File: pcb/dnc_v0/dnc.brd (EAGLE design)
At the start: 100 x 80 mm, 1 part

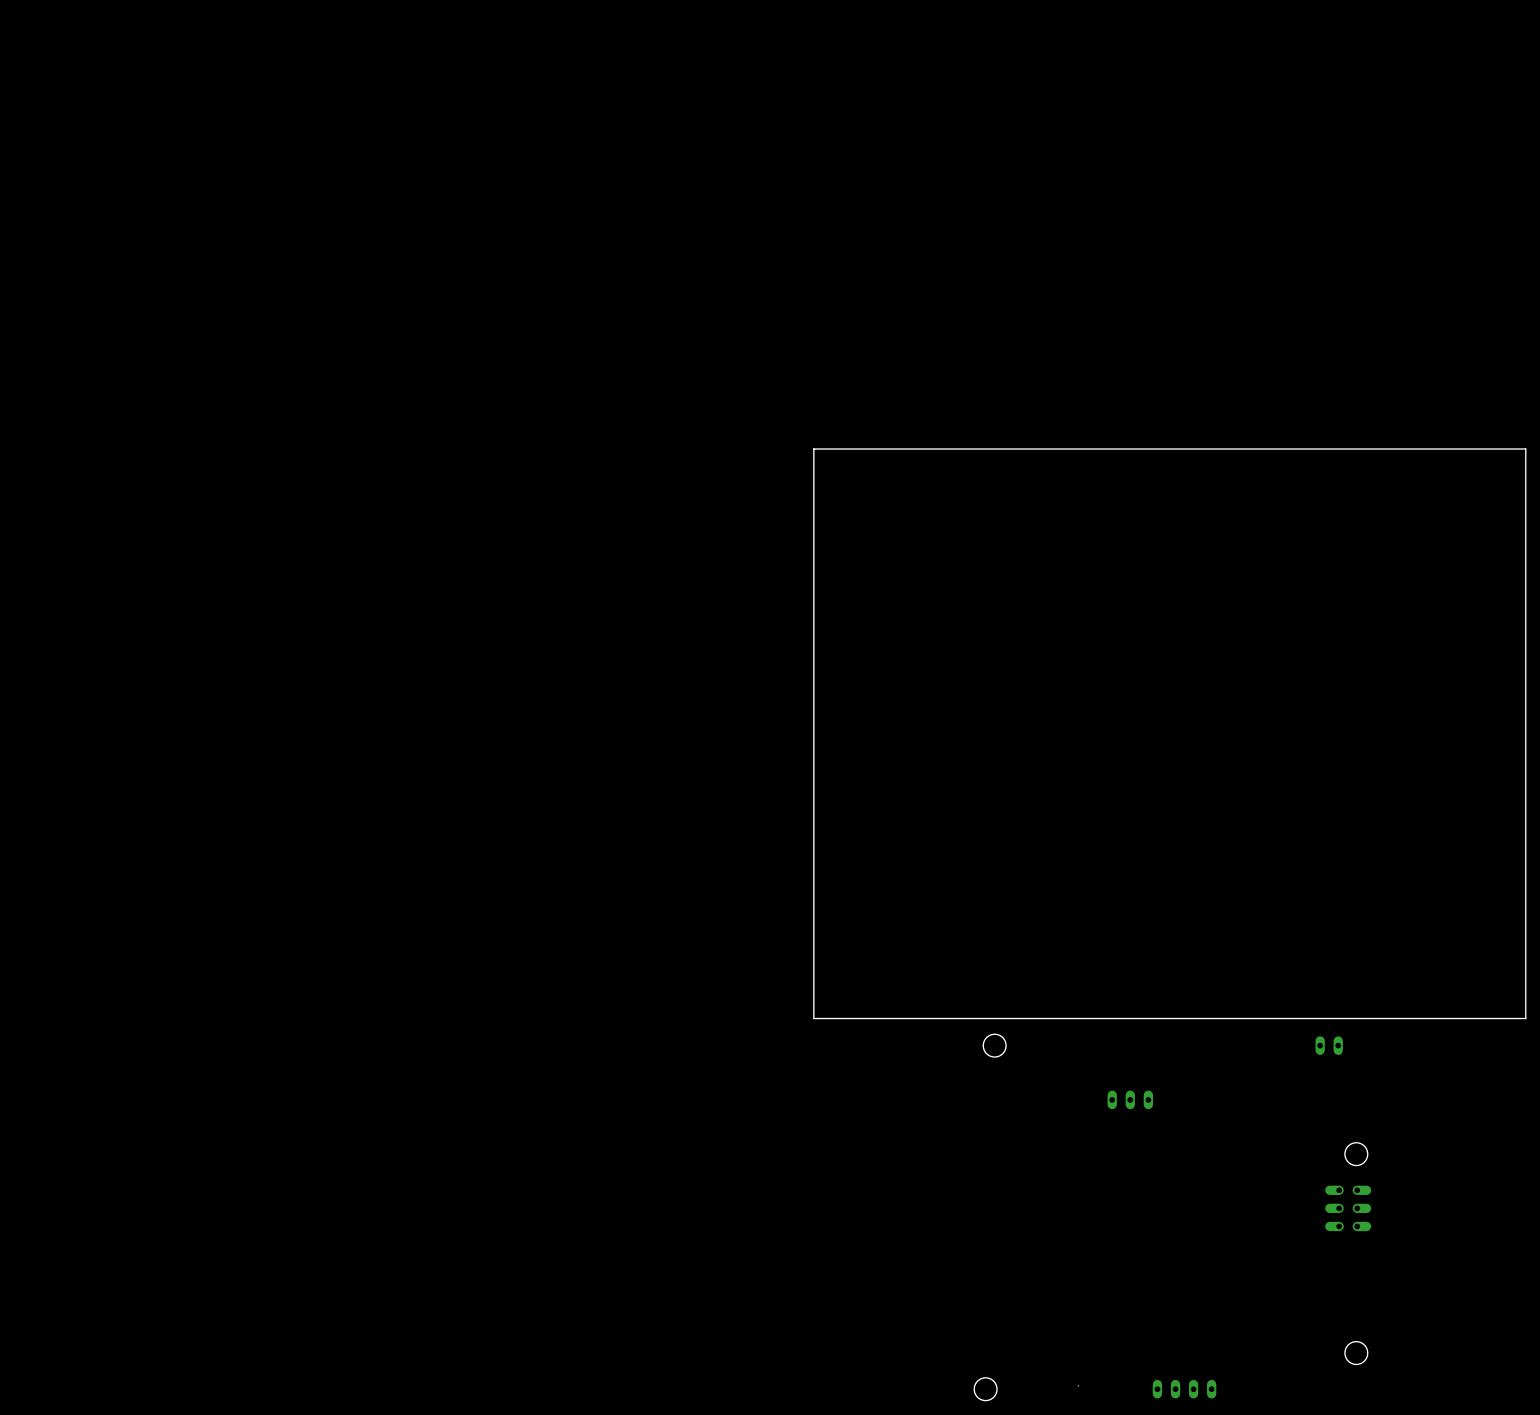
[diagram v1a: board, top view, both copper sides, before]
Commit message: changement de plie de package + liste des composants en stock
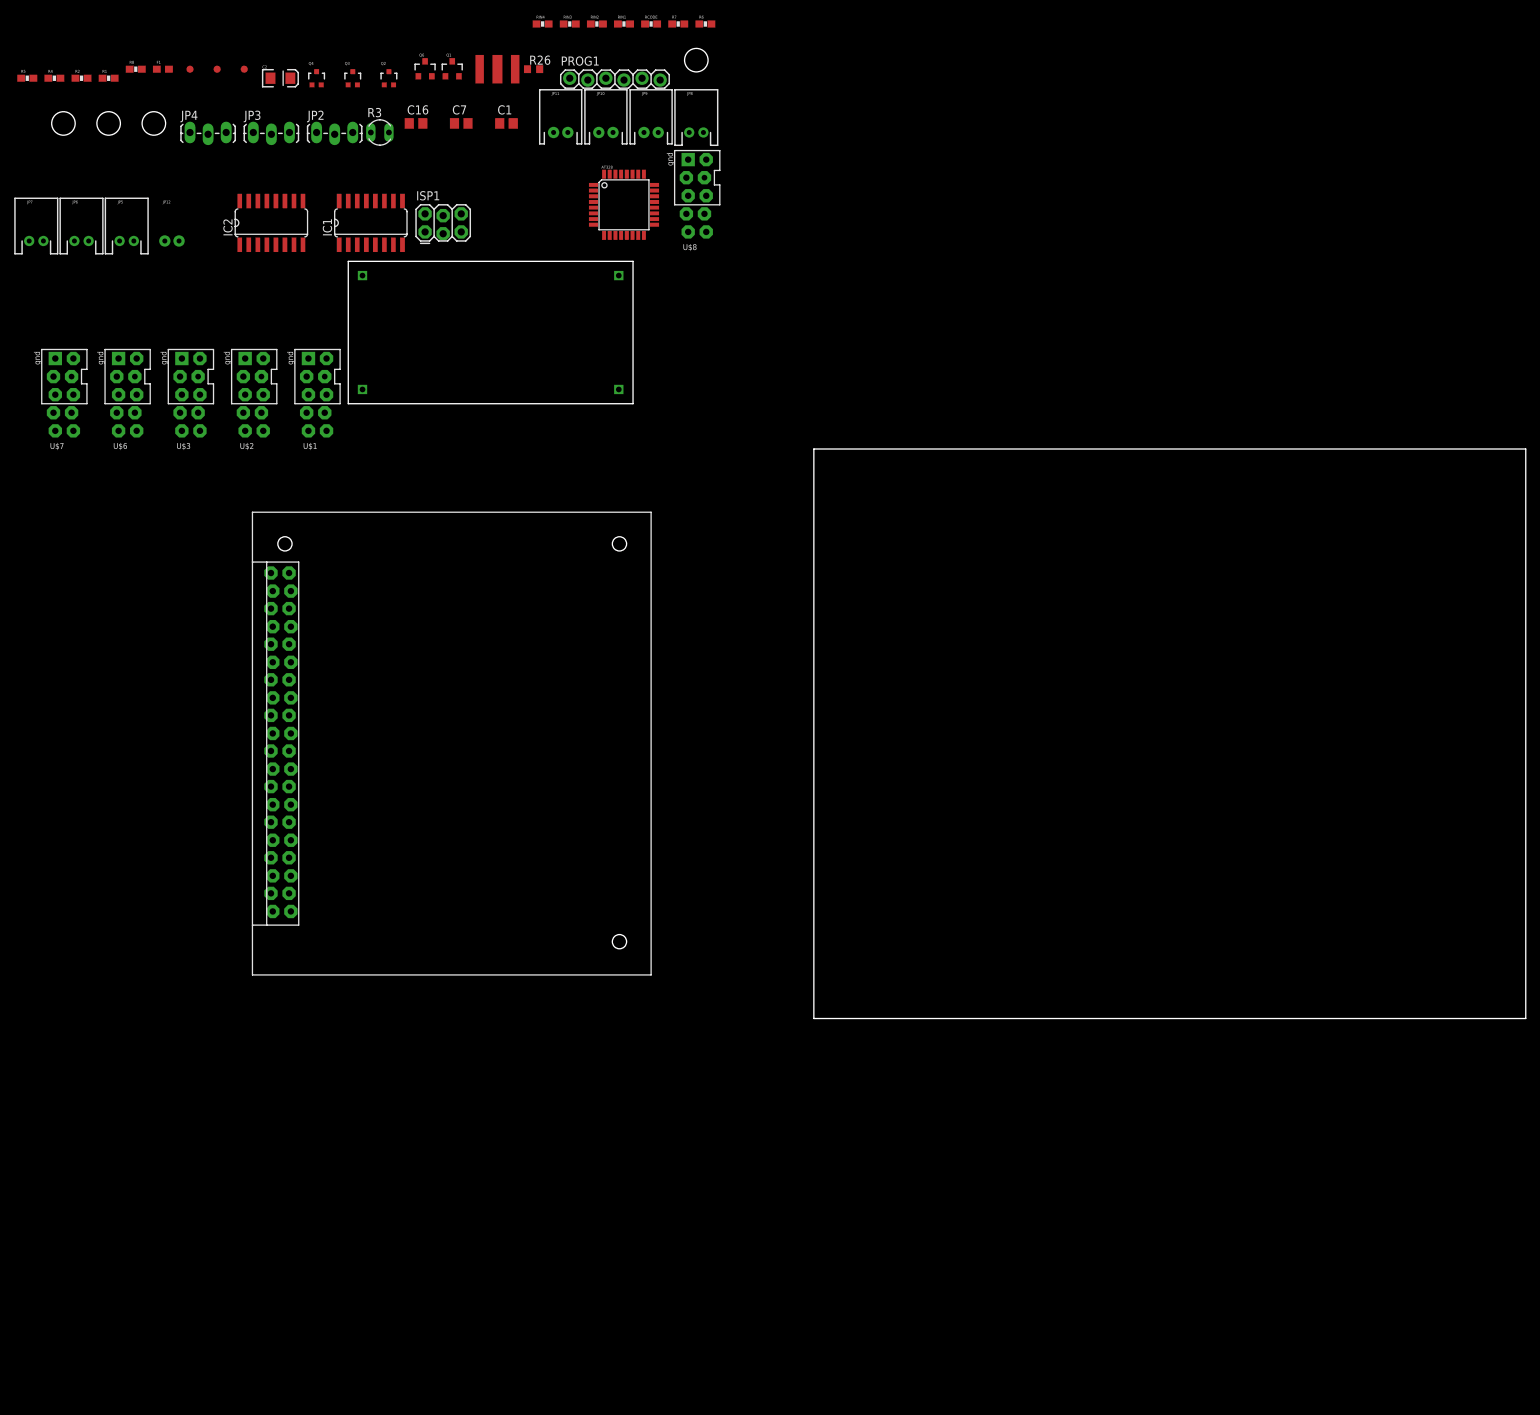
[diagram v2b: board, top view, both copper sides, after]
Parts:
- added 8MHZ: RESONATOR, pierre_vv:RESONATOR_7MM
- added AT328: ATMEGA168, SparkFun:TQFP32-08
- added C1, C16, C7: 0.1uF, rcl:C0805
- added C2: 10uF, SparkFun:EIA3216
- added F1: PTC0603, SparkFun-PowerIC:0603
- added IC1, IC2: 74HC595D, 74xx-eu:SO16
- added ISP1: AVR_SPI_PRG_62X3_LOCK, SparkFun:2X3_LOCK
- added JP10, JP11, JP9: M02JST-PTH-2, SparkFun-Connectors:JST-2-PTH
- added JP12: M02-JST-2-PTH-NO_SILK, SparkFun-Connectors:JST-2-PTH-NS
- added JP13, JP14, JP19: FIDUCIAL1X2.5, SparkFun:FIDUCIAL-1X2.5
- added JP15, JP16, JP17, JP18: STAND-OFF, SparkFun:STAND-OFF
- added JP2, JP3, JP4: (no value), SparkFun:1X03_LOCK_LONGPADS
- added JP5, JP6, JP7, JP8: (no value), SparkFun:JST-2-PTH
- added PROG1: (no value), SparkFun:1X06_LOCK
- added Q1, Q6: 200mA/50V, SparkFun-DiscreteSemi:SOT23-3
- added Q2, Q3, Q4: TSM2306CX, SparkFun-DiscreteSemi:SOT323
- added R1, R2, R4, R5, R6, R7, RCODE, RIN1, RIN2, RIN3, RIN4: (no value), SparkFun-Passives:0603-RES
- added R26: 10K, rcl:R0603
- added R3: (no value), ptc-ntc:P679
- added R8: 100K, SparkFun-Passives:0603-RES
- added U$2, U$3, U$6, U$7, U$8: EXT-DNC, pierre_vv:EXTPINDNC
- added U$4: RASPIA+, pierre_vv:RASPIA+
- added U$5: DC/DC_SEED, pierre_vv:DC/DC_SEED
- U$1: value YUNBOARD_CONNECT -> EXT-DNC; device pierre_vv:YUN-RECEIVE -> pierre_vv:EXTPINDNC
- moved U$1 162.6 mm to (-69.8, 87.6)
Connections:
- new net /CS_EXT_1: U$3./RESET
- new net /CS_EXT_2: U$1./RESET
- new net /CS_EXT_3: U$2./RESET
- new net /CS_EXT_4: U$6./RESET
- new net /CS_EXT_5: U$7./RESET
- new net /CS_EXT_6: U$8./RESET
- new net 3.3: U$1.3.3, U$2.3.3, U$3.3.3, U$6.3.3, U$7.3.3, U$8.3.3
- new net 5V: AT328.18, AT328.4, AT328.6, C16.1, ISP1.2, JP2.2, JP3.2, JP4.2, PROG1.4, R26.2, R3.1, U$4.2, U$4.4, U$5.OUT+
- new net ACTIVE_ANALOG_RAW: Q1.1, R8.2
- new net ACTIVE_ANALOG_TEMP: Q6.1
- new net ACTIVE_OUT_POWER_1: Q3.1, U$4.36
- new net ACTIVE_OUT_POWER_2: Q2.1, U$4.38
- new net ACTIVE_OUT_POWER_3: Q4.1, U$4.40
- new net ANALOG_IN_1: JP2.3
- new net ANALOG_IN_2: JP3.3
- new net ANALOG_IN_3: JP4.3
- new net ANALOG_RAW: Q1.2, R2.2
- new net ANALOG_TEMP: Q6.2, R4.1
- new net AREF: AT328.20, C7.1
- new net ATMEGA_CS: U$4.6
- new net CODE: RCODE.1, U$1.RETOURANALOG, U$2.RETOURANALOG, U$3.RETOURANALOG, U$6.RETOURANALOG, U$7.RETOURANALOG, U$8.RETOURANALOG
- new net DTR: C1.1, PROG1.1
- new net GND: 8MHZ.2, AT328.21, AT328.3, AT328.5, C16.2, C2.C, C7.2, IC1.8, IC2.8, ISP1.6, JP10.2, JP11.2, JP12.2, JP2.1, JP3.1, JP4.1, JP9.2, PROG1.5, PROG1.6, R2.1, R4.2, R5.1, R6.1, R7.1, R8.1, RCODE.2, RIN1.1, RIN2.1, RIN3.1, RIN4.1, U$1.1_GND, U$2.1_GND, U$3.1_GND, U$4.14, U$4.20, U$4.25, U$4.30, U$4.34, U$4.39, U$4.9, U$5.IN-, U$5.OUT-, U$6.1_GND, U$7.1_GND, U$8.1_GND
- new net IN_1: JP5.2, RIN1.2, U$4.3
- new net IN_2: JP6.2, RIN2.2, U$4.5
- new net IN_3: JP7.2, RIN3.2, U$4.11
- new net IN_4: JP8.2, RIN4.2, U$4.13
- new net MISO: ISP1.1, U$1.MISO, U$2.MISO, U$3.MISO, U$4.21, U$6.MISO, U$7.MISO, U$8.MISO
- new net MOSI: ISP1.4, U$1.MOSI, U$2.MOSI, U$3.MOSI, U$4.19, U$6.MOSI, U$7.MOSI, U$8.MOSI
- new net N$10: U$8.FREE
- new net N$11: Q6.3, R3.2
- new net N$12: F1.1, JP12.1
- new net N$15: U$4.7
- new net N$18: U$4.15
- new net N$21: U$3.FREE
- new net N$23: U$4.27
- new net N$26: R6.2
- new net N$27: U$4.35
- new net N$28: U$4.37
- new net N$29: Q4.2, R7.2
- new net N$3: Q1.3, R1.1
- new net N$31: U$4.8
- new net N$32: U$4.10
- new net N$33: U$4.12
- new net N$34: U$4.16
- new net N$35: U$4.18
- new net N$36: U$4.22
- new net N$37: U$4.24
- new net N$38: U$4.26
- new net N$39: U$4.28
- new net N$4: U$1.FREE
- new net N$40: U$4.32
- new net N$43: 8MHZ.1, AT328.7
- new net N$44: 8MHZ.3, AT328.8
- new net N$5: U$2.FREE
- new net N$7: IC1.9, IC2.14
- new net N$8: U$6.FREE
- new net N$9: U$7.FREE
- new net OUT_POWER_1: JP9.1, Q3.2
- new net OUT_POWER_2: JP10.1, Q2.2, R5.2
- new net OUT_POWER_3: JP11.1
- new net RAW: C2.A, F1.2, IC1.16, IC2.16, Q2.3, Q3.3, Q4.3, R1.2, U$1.RAW, U$2.RAW, U$3.RAW, U$5.IN+, U$6.RAW, U$7.RAW, U$8.RAW
- new net REG_RCK: IC1.12, IC2.12, U$4.31
- new net REG_SCK: IC1.11, IC2.11, U$4.29
- new net REG_VAL: IC1.14, U$4.33
- new net RESET: AT328.29, C1.2, ISP1.5, R26.1
- new net RST1: IC1.15
- new net RST10: IC2.1
- new net RST11: IC2.2
- new net RST12: IC2.3
- new net RST13: IC2.4
- new net RST14: IC2.5
- new net RST15: IC2.6
- new net RST16: IC2.7
- new net RST2: IC1.1
- new net RST3: IC1.2
- new net RST4: IC1.3
- new net RST5: IC1.4
- new net RST6: IC1.5
- new net RST7: IC1.6
- new net RST8: IC1.7
- new net RST9: IC2.15
- new net RX-I: PROG1.3
- new net SCK: ISP1.3, U$1.SCK, U$2.SCK, U$3.SCK, U$4.23, U$6.SCK, U$7.SCK, U$8.SCK
- new net TX-O: PROG1.2
- new net VCC: JP5.1, JP6.1, JP7.1, JP8.1, U$1.VCC, U$2.VCC, U$3.VCC, U$4.1, U$4.17, U$6.VCC, U$7.VCC, U$8.VCC
